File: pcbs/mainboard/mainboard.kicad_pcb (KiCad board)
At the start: 4 copper layers, 59 x 93 mm, 49 parts, among them J1 USB_B_Micro, J10 STAT_LED, J11 nReset_Button, J12 VBUS, J2 key_row_0, J3 key_row_1, J4 key_row_2, J5 ICSP, J6 JTAG, J7 Crank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

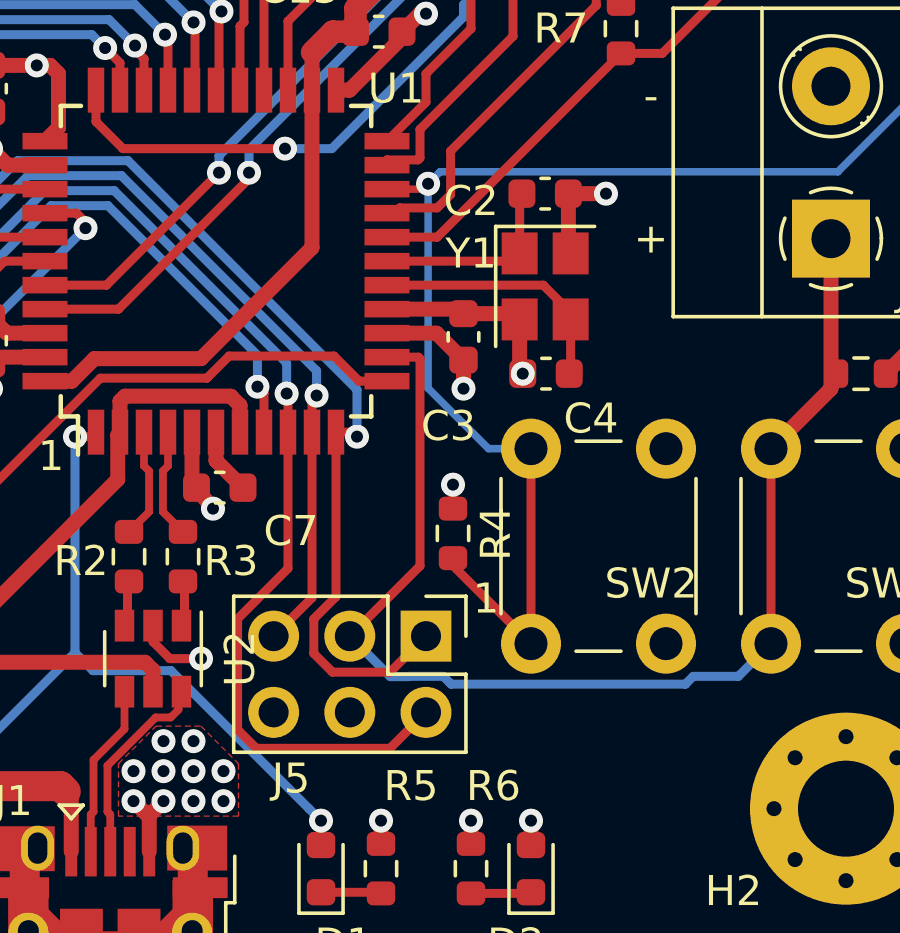
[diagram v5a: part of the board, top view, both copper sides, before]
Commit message: Add copper pour keepout under crystal
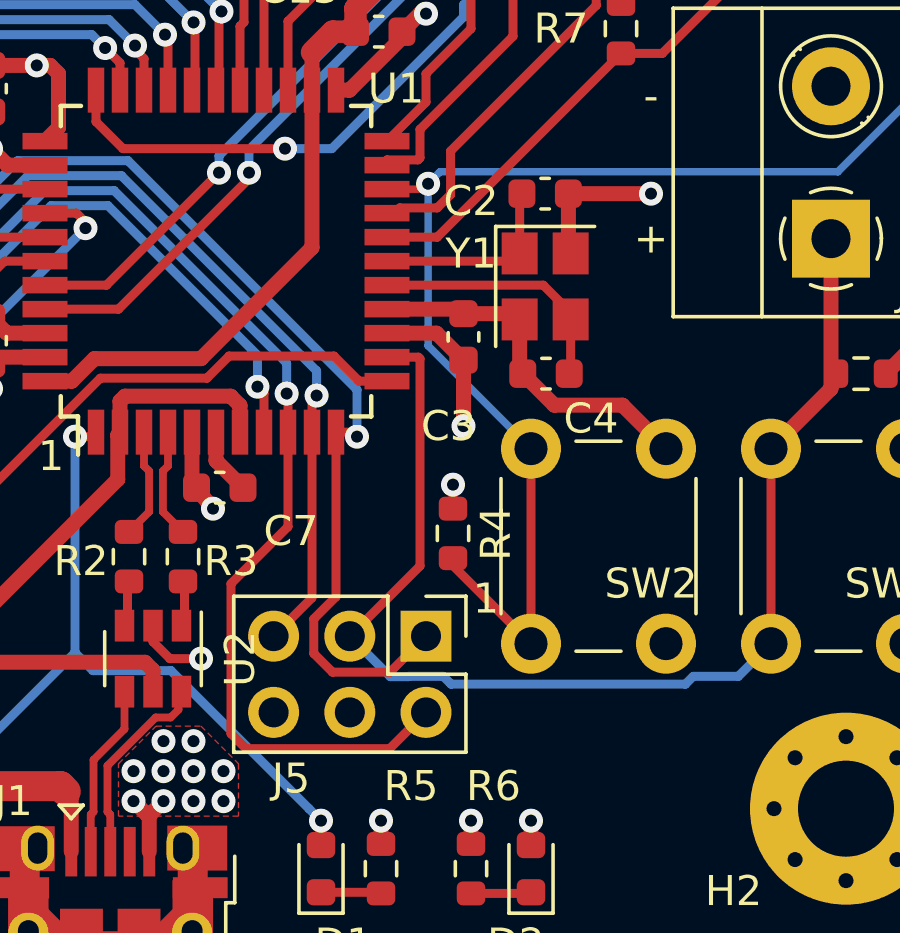
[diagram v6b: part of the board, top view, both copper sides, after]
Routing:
- net GND: track 53.4 -> 60.7 mm, vias 24 -> 23
- net +3V3: track 40.3 -> 41.5 mm
- net GPIO6_HWB: track 96.4 -> 95.6 mm
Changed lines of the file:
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@@
     (thickness 1.6)
     (drawings 38)
-    (tracks 707)
+    (tracks 708)
     (zones 0)
     (modules 49)
@@
   )
   (setup
-    (last_trace_width 0.3)
+    (last_trace_width 0.5)
     (user_trace_width 0.3)
     (user_trace_width 0.5)
@@
   (gr_line (start 99 29) (end 158 29) (layer Edge.Cuts) (width 0.05))
   (gr_line (start 99 118) (end 99 29) (layer Edge.Cuts) (width 0.05))
-  (via (at 145.5 95.5) (size 0.8) (drill 0.4) (layers F.Cu B.Cu) (net 1))
-  (segment (start 144.247 95.5) (end 145.5 95.5) (width 0.5) (layer F.Cu) (net 1))
   (segment (start 144.247 97.417) (end 144.322 97.492) (width 0.5) (layer F.Cu) (net 1))
   (segment (start 144.247 95.5) (end 144.247 97.417) (width 0.5) (layer F.Cu) (net 1))
@@
   (segment (start 140.6 99.35) (end 138.2 99.35) (width 0.5) (layer F.Cu) (net 1))
   (segment (start 140.75 99.5) (end 140.6 99.35) (width 0.5) (layer F.Cu) (net 1))
-  (via (at 142.725 101.5) (size 0.8) (drill 0.4) (layers F.Cu B.Cu) (net 1))
   (segment (start 114.8 86.9) (end 114.8 87.725008) (width 0.75) (layer F.Cu) (net 1))
   (segment (start 114.8 87.725008) (end 114.550009 87.974999) (width 0.75) (layer F.Cu) (net 1))
@@
   (segment (start 139.85 100.15) (end 138.2 100.15) (width 0.5) (layer F.Cu) (net 2))
   (segment (start 140.75 101.05) (end 139.85 100.15) (width 0.5) (layer F.Cu) (net 2))
-  (via (at 140.75 102) (size 0.8) (drill 0.4) (layers F.Cu B.Cu) (net 2))
-  (segment (start 140.75 101.05) (end 140.75 102) (width 0.5) (layer F.Cu) (net 2))
   (via (at 146.1 88) (size 0.8) (drill 0.4) (layers F.Cu B.Cu) (net 2))
   (segment (start 146 88.1) (end 146.1 88) (width 0.3) (layer F.Cu) (net 2))
@@
   (segment (start 130.4 110.435002) (end 130.964998 111) (width 0.3) (layer F.Cu) (net 1))
   (segment (start 130.4 109.9) (end 130.4 110.435002) (width 0.3) (layer F.Cu) (net 1))
+  (via (at 147 95.5) (size 0.8) (drill 0.4) (layers F.Cu B.Cu) (net 1))
+  (segment (start 144.247 95.5) (end 147 95.5) (width 0.5) (layer F.Cu) (net 1))
+  (segment (start 143.774999 102.549999) (end 142.725 101.5) (width 0.5) (layer F.Cu) (net 1))
+  (segment (start 146.049999 102.549999) (end 143.774999 102.549999) (width 0.5) (layer F.Cu) (net 1))
+  (segment (start 147.5 104) (end 146.049999 102.549999) (width 0.5) (layer F.Cu) (net 1))
   (via (at 115.475 110.775) (size 0.8) (drill 0.4) (layers F.Cu B.Cu) (net 2))
   (via (at 114.5 110.775) (size 0.8) (drill 0.4) (layers F.Cu B.Cu) (net 2))
@@
   (segment (start 155.575 100.75) (end 154.825 101.5) (width 0.5) (layer F.Cu) (net 2))
   (segment (start 155.749996 100.75) (end 155.575 100.75) (width 0.5) (layer F.Cu) (net 2))
+  (via (at 140.75 103.25) (size 0.8) (drill 0.4) (layers F.Cu B.Cu) (net 2))
+  (segment (start 140.75 101.05) (end 140.75 103.25) (width 0.5) (layer F.Cu) (net 2))
   (segment (start 119.233164 113.775) (end 119 113.775) (width 1) (layer F.Cu) (net 7))
   (segment (start 116.275 113.775) (end 116.25 113.75) (width 1) (layer F.Cu) (net 7))
@@
   (segment (start 138.31 111.6) (end 138.913998 111.6) (width 0.3) (layer B.Cu) (net 43))
   (segment (start 136.96 110.25) (end 138.31 111.6) (width 0.3) (layer B.Cu) (net 43))
-  (segment (start 138.299999 113.990001) (end 139.5 112.79) (width 0.3) (layer F.Cu) (net 44))
-  (segment (start 133.843999 113.990001) (end 138.299999 113.990001) (width 0.3) (layer F.Cu) (net 44))
-  (segment (start 133.219999 113.366001) (end 133.843999 113.990001) (width 0.3) (layer F.Cu) (net 44))
-  (segment (start 134.9 107.993998) (end 133.219999 109.673999) (width 0.3) (layer F.Cu) (net 44))
-  (segment (start 133.219999 109.673999) (end 133.219999 113.366001) (width 0.3) (layer F.Cu) (net 44))
-  (segment (start 134.9 103.45) (end 134.9 107.993998) (width 0.3) (layer F.Cu) (net 44))
   (via (at 134.854963 102.162518) (size 0.8) (drill 0.4) (layers F.Cu B.Cu) (net 44))
   (segment (start 134.9 102.207555) (end 134.854963 102.162518) (width 0.3) (layer F.Cu) (net 44))
@@
   (segment (start 123.895562 98.3) (end 119.237071 98.3) (width 0.3) (layer B.Cu) (net 44))
   (segment (start 119.237071 98.3) (end 118.987142 98.050071) (width 0.3) (layer B.Cu) (net 44))
+  (segment (start 138.29 114) (end 139.5 112.79) (width 0.3) (layer F.Cu) (net 44))
+  (segment (start 133.5 114) (end 138.29 114) (width 0.3) (layer F.Cu) (net 44))
+  (segment (start 133 108.5) (end 133 113.5) (width 0.3) (layer F.Cu) (net 44))
+  (segment (start 133 113.5) (end 133.5 114) (width 0.3) (layer F.Cu) (net 44))
+  (segment (start 134.9 106.6) (end 133 108.5) (width 0.3) (layer F.Cu) (net 44))
+  (segment (start 134.9 103.45) (end 134.9 106.6) (width 0.3) (layer F.Cu) (net 44))
   (segment (start 138.299999 111.450001) (end 139.5 110.25) (width 0.3) (layer F.Cu) (net 45))
   (segment (start 136.383999 111.450001) (end 138.299999 111.450001) (width 0.3) (layer F.Cu) (net 45))
@@
   (segment (start 139.389324 95.35) (end 139.569662 95.169662) (width 0.25) (layer F.Cu) (net 52))
   (via (at 139.569662 95.169662) (size 0.8) (drill 0.4) (layers F.Cu B.Cu) (net 52))
-  (segment (start 139.569662 101.983875) (end 139.569662 95.169662) (width 0.25) (layer B.Cu) (net 52))
   (segment (start 138.2 95.35) (end 139.389324 95.35) (width 0.25) (layer F.Cu) (net 52))
   (segment (start 153.230337 94.769663) (end 139.969661 94.769663) (width 0.25) (layer B.Cu) (net 52))
   (segment (start 156 40.52) (end 156 92) (width 0.25) (layer B.Cu) (net 52))
   (segment (start 139.969661 94.769663) (end 139.569662 95.169662) (width 0.25) (layer B.Cu) (net 52))
-  (segment (start 143 104) (end 141.585787 104) (width 0.25) (layer B.Cu) (net 52))
-  (segment (start 141.585787 104) (end 139.569662 101.983875) (width 0.25) (layer B.Cu) (net 52))
   (segment (start 153 37.52) (end 156 40.52) (width 0.25) (layer B.Cu) (net 52))
   (segment (start 156 92) (end 153.230337 94.769663) (width 0.25) (layer B.Cu) (net 52))
+  (segment (start 143 104) (end 139.569662 100.569662) (width 0.25) (layer B.Cu) (net 52))
+  (segment (start 139.569662 100.569662) (end 139.569662 95.169662) (width 0.25) (layer B.Cu) (net 52))
   (via (at 133.600002 94.8) (size 0.8) (drill 0.4) (layers F.Cu B.Cu) (net 53))
   (segment (start 133.600002 94.999998) (end 133.600002 94.8) (width 0.3) (layer F.Cu) (net 53))
@@
       )
     )
+  )
+  (zone (net 0) (net_name "") (layers In1.Cu In2.Cu) (hatch edge 0.508)
+    (connect_pads (clearance 0.508))
+    (min_thickness 0.254)
+    (keepout (tracks allowed) (vias allowed) (copperpour not_allowed))
+    (fill (arc_segments 32) (thermal_gap 0.4) (thermal_bridge_width 0.508))
+    (polygon
+      (pts
+        (xy 145.5 102.5) (xy 141.5 102.5) (xy 141.5 99) (xy 137 99) (xy 137 97.5)
+        (xy 141.5 97.5) (xy 141.5 94.5) (xy 145.5 94.5)
+      )
+    )
